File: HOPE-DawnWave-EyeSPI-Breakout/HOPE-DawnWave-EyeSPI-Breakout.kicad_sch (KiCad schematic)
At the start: 1 part, among them X1 EYE_SPI_DISPLAY_FLIP

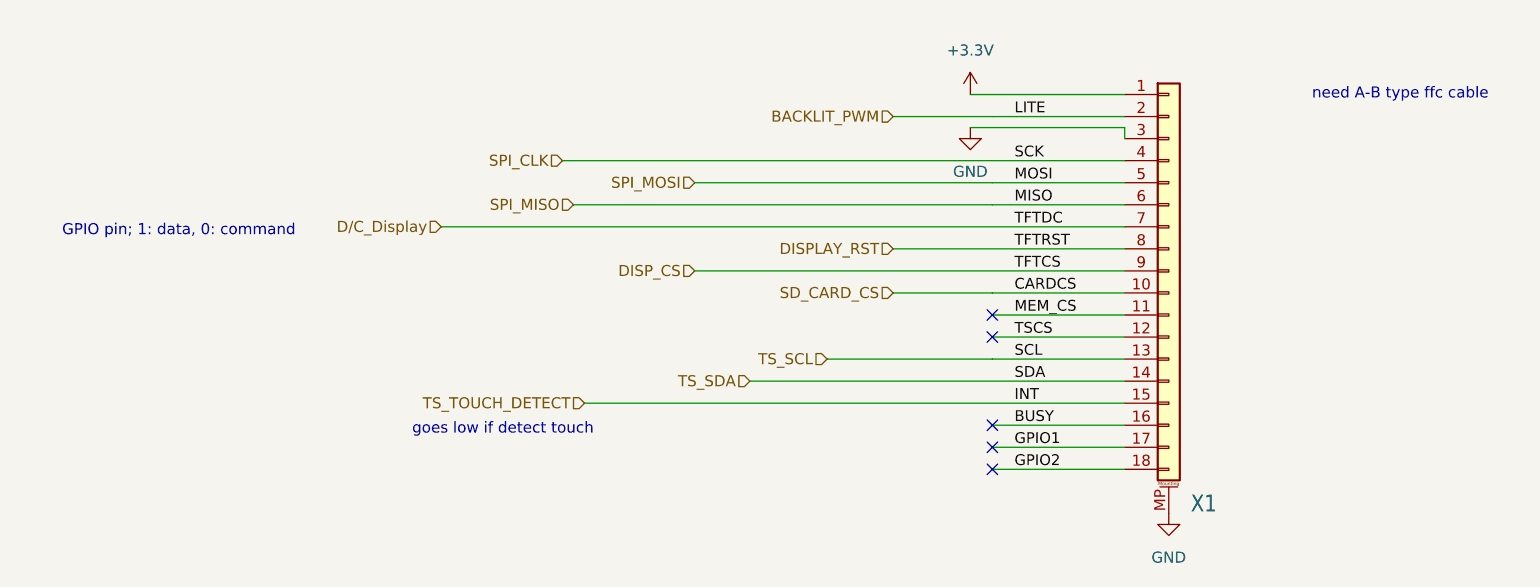
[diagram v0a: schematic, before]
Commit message: corrected eyespi connector wiring and added a 2.54mm pitch header to break it out in case something bad happens
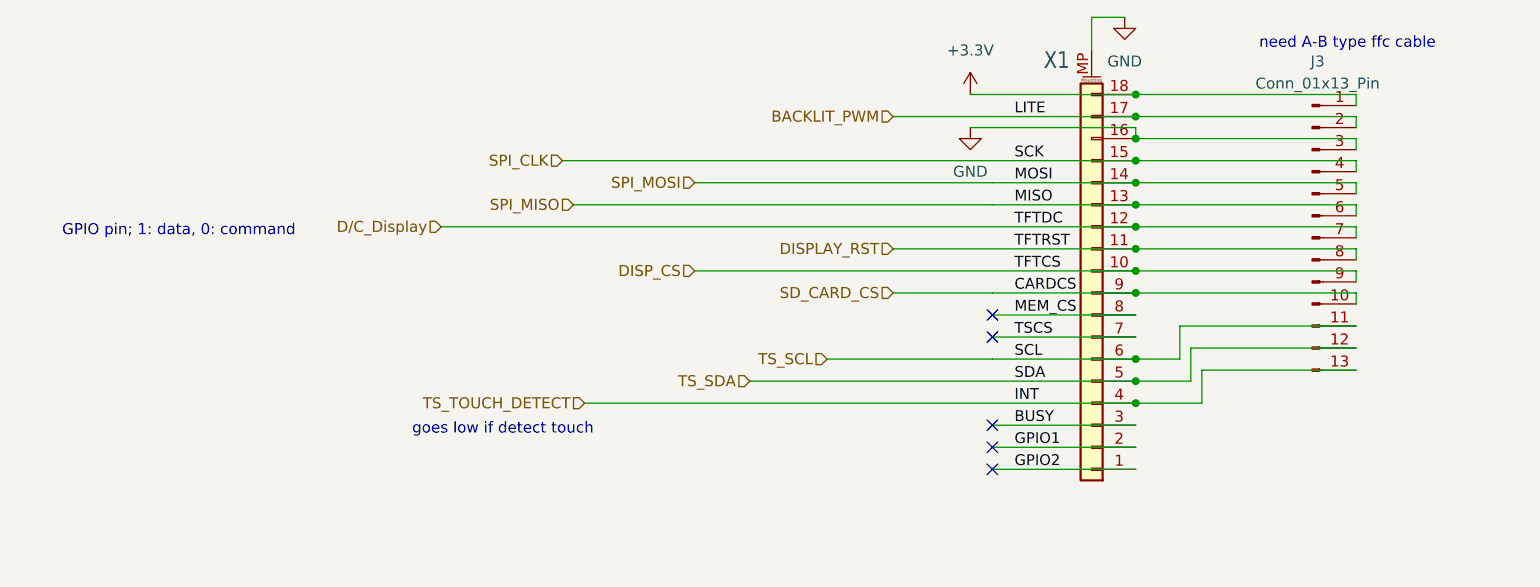
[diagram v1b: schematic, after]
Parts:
- added J3: Conn_01x13_Pin, Connector_PinHeader_2.54mm:PinHeader_1x13_P2.54mm_Vertical, symbol Connector:Conn_01x13_Pin
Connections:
- net +3.3V: now also X1.18 (Pin_18), J3.1 (Pin_1); no longer X1.1 (Pin_1)
- net BACKLIT_PWM: now also X1.17 (Pin_17), J3.2 (Pin_2); no longer X1.2 (Pin_2)
- net BUSY: now also X1.3 (Pin_3); no longer X1.16 (Pin_16)
- net DISPLAY_RST: now also X1.11 (Pin_11), J3.8 (Pin_8); no longer X1.8 (Pin_8)
- net DISP_CS: now also X1.10 (Pin_10), J3.9 (Pin_9); no longer X1.9 (Pin_9)
- net D/C_Display: now also X1.12 (Pin_12), J3.7 (Pin_7); no longer X1.7 (Pin_7)
- net GND: now also X1.16 (Pin_16), J3.3 (Pin_3); no longer X1.3 (Pin_3)
- net GPIO1: now also X1.2 (Pin_2); no longer X1.17 (Pin_17)
- net GPIO2: now also X1.1 (Pin_1); no longer X1.18 (Pin_18)
- net MEM_CS: now also X1.8 (Pin_8); no longer X1.11 (Pin_11)
- net SD_CARD_CS: now also X1.9 (Pin_9), J3.10 (Pin_10); no longer X1.10 (Pin_10)
- net SPI_CLK: now also X1.15 (Pin_15), J3.4 (Pin_4); no longer X1.4 (Pin_4)
- net SPI_MISO: now also X1.13 (Pin_13), J3.6 (Pin_6); no longer X1.6 (Pin_6)
- net SPI_MOSI: now also X1.14 (Pin_14), J3.5 (Pin_5); no longer X1.5 (Pin_5)
- net TSCS: now also X1.7 (Pin_7); no longer X1.12 (Pin_12)
- net TS_SCL: now also X1.6 (Pin_6), J3.11 (Pin_11); no longer X1.13 (Pin_13)
- net TS_SDA: now also X1.5 (Pin_5), J3.12 (Pin_12); no longer X1.14 (Pin_14)
- net TS_TOUCH_DETECT: now also X1.4 (Pin_4), J3.13 (Pin_13); no longer X1.15 (Pin_15)
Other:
- moved on the sheet: X1
